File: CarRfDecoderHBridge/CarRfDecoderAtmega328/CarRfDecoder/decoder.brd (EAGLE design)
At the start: 98.7 x 80 mm, 52 parts, among them T1 BC847, T2 BC847, T3 IRLML6402, U2 RFM69CW, U3 MCP73831, U4 ATMEGA328P, U6 MIC5219 3.3V, Y1 16MHZ

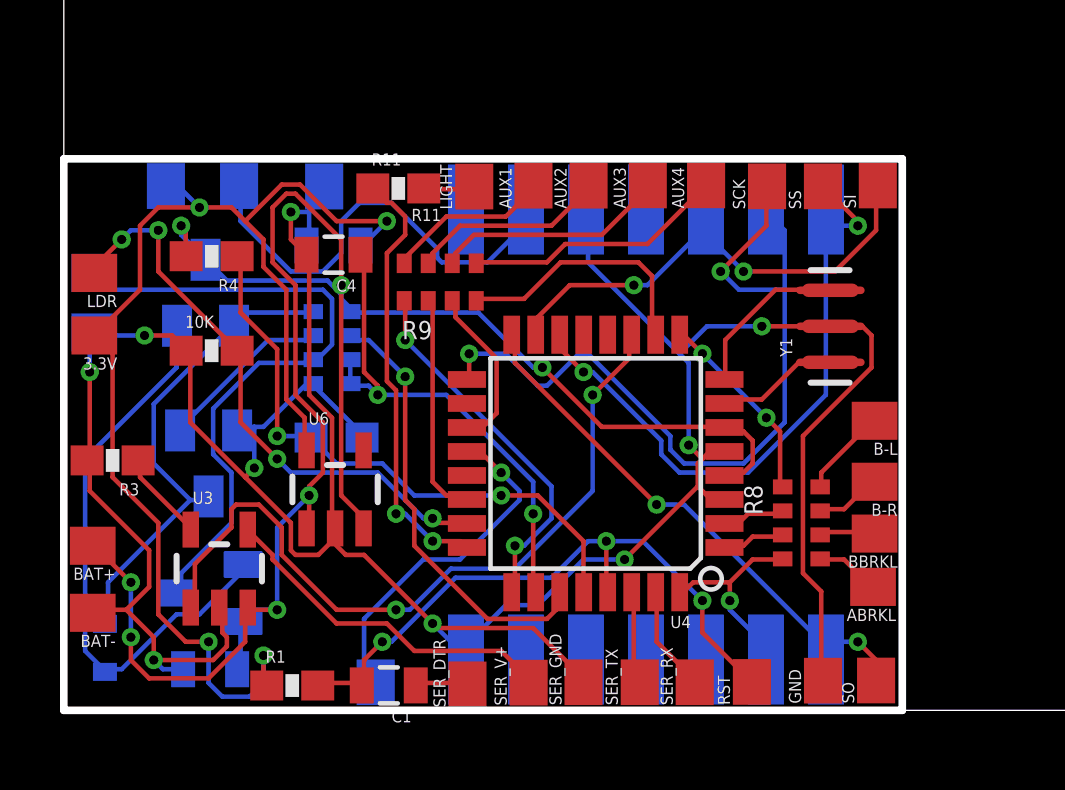
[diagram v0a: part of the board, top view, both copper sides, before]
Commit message: Add Board with hbridge
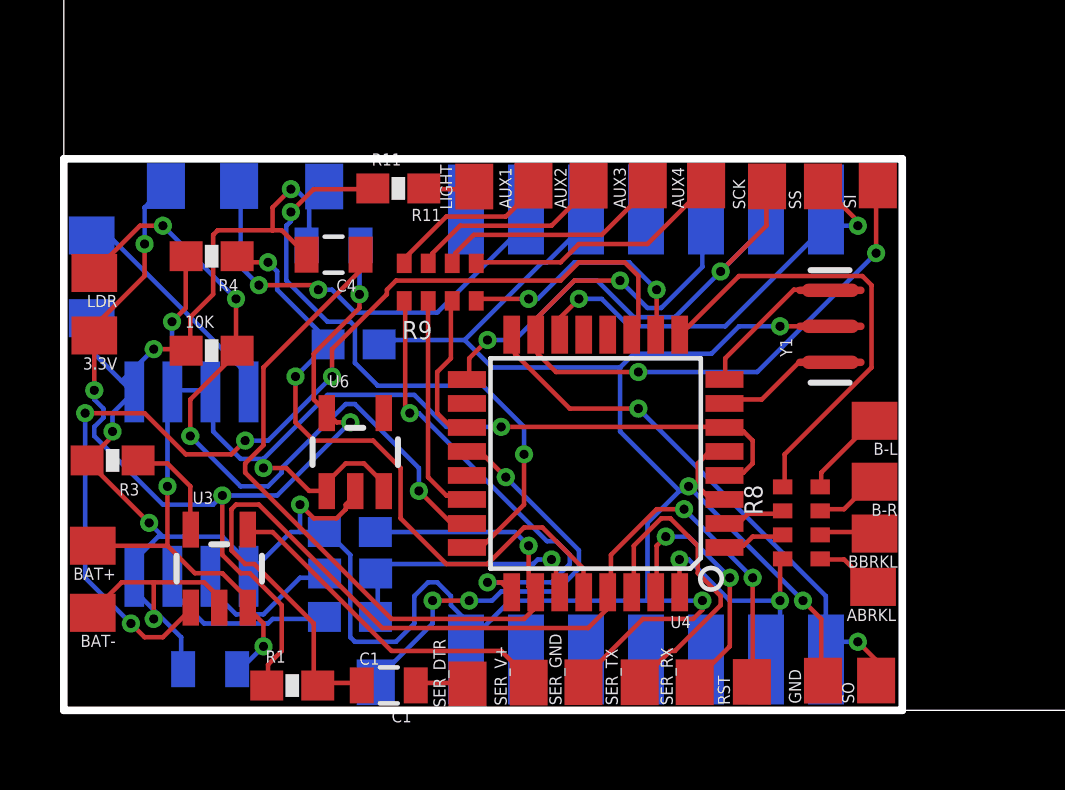
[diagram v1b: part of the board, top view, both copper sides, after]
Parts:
- removed D1: (no value), adafruit:SOD-523
- removed T1, T2: BC847, transistor:SOT23
- removed T3: IRLML6402, we-transistor:SOT23
- added MDRIVER: L9110S, h-bridge-l9119s:SO08
- added R2: 2k2, SparkFun-Resistors:0603-RES
- added R7: 0, SparkFun-Resistors:0603-RES
- R6: value 2k2 -> 0; device SparkFun-Resistors:0603-ARV -> SparkFun-Resistors:0603-RES
- moved R6 7.55 mm to (10.8, 4.56), turned to 0 degrees
- moved R5 3.16 mm to (10.9, 12.2)
- moved U6 1.41 mm to (11.0, 8.61)
- moved MOTOR 1.25 mm to (2.20, 15.8)
- moved MOTORGND 0.48 mm to (2.20, 13.1)
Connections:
- removed net N$14: D1.A, T1.2, T3.1
- removed net N$15: MOTOR.1, R6.6, T3.3
- removed net N$17: R6.7, T2.1
- removed net N$19: D1.K, R6.8, T1.1, T2.3
- new net N$6: MDRIVER.6, R6.2
- new net N$7: MDRIVER.7, R7.2
- new net OB: MDRIVER.4, MOTOR.1
- net A3: now also R2.1; no longer R6.3, R6.4
- net A4: now also R6.1, R7.1; no longer R6.2
- net BAT+: now also MDRIVER.2, MDRIVER.3; no longer R6.1, T1.3, T3.2
- net GND: now also MDRIVER.1, MDRIVER.5, MDRIVER.8, R2.2; no longer R6.5, T2.2
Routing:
- net N$15: track 21.9 -> 0.00 mm
- net BAT+: track 68.7 -> 49.0 mm, vias 7 -> 5
- net N$14: track 19.3 -> 0.00 mm
- net N$19: track 16.4 -> 0.00 mm
- net N$5: track 21.3 -> 35.1 mm, vias 3 -> 2
- net A3: track 16.9 -> 28.2 mm, vias 2 -> 1
- net SCK: track 27.8 -> 17.5 mm
- net D7: track 25.4 -> 34.8 mm, vias 2 -> 4
- net BL: track 6.59 -> 15.3 mm, vias 2 -> 0
- net MOSI: track 17.2 -> 25.6 mm, vias 2 -> 3
- net VCC: track 42.9 -> 35.0 mm, vias 4 -> 5
- net OB: track 0.00 -> 7.75 mm
- net GND: track 108.4 -> 116.0 mm, vias 9 -> 10
- net RX: track 3.09 -> 10.6 mm
- net SS: track 22.0 -> 15.4 mm
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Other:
- board text added: "C1"
- board text added: "R6"
- board text added: "R7"

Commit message: bug fixes and better board routing
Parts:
- removed SS: (no value), wirepad:SMD1,27-2,54
- moved AUX4 18.3 mm to (14.7, 0.96)
- moved AUX3 17.0 mm to (16.8, 0.96)
- moved AUX1 17.0 mm to (20.7, 0.96)
- moved AUX2 16.6 mm to (18.7, 0.92)
- moved SO 14.6 mm to (28.3, 15.6), turned to 90 degrees
- moved R9 10.0 mm to (13.1, 4.28), turned to 180 degrees
- moved SER_V+ 6.04 mm to (10.7, 0.89)
- moved SER_GND 5.98 mm to (12.6, 0.94)
- moved R7 5.97 mm to (4.85, 3.61), turned to 90 degrees
- moved C1 5.95 mm to (6.15, 0.80)
- moved SER_DTR 5.87 mm to (8.86, 0.92)
- moved R1 5.72 mm to (3.16, 0.81)
- moved R6 4.39 mm to (6.53, 3.60), turned to 90 degrees
- moved SER_RX 4.16 mm to (26.5, 0.94)
- moved SER_TX 4.16 mm to (24.6, 0.94)
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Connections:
- removed net AX1: R9.1, U4.25
- removed net AX2: R9.2, U4.22
- removed net AX3: R9.3, U4.19
- removed net AX4: R9.4, U4.10
- new net A2: R9.4, U4.25
- new net A6: C4.1, R2.1, U4.19
- new net A7: R4.1, R5.2, U4.22
- new net D6: R9.1, U4.10
- net A1: now also U3.1; no longer R11.1
- net A3: now also R9.3; no longer C4.1, R2.1
- net A5: now also R9.2; no longer R4.1, R5.2
- net D7: now also R11.1; no longer U3.1
- net SS: no longer SS.1
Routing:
- net D7: track 34.8 -> 10.3 mm, vias 4 -> 0
- net A5: track 22.1 -> 6.46 mm, vias 2 -> 0
- net AX1: track 15.3 -> 0.00 mm, vias 2 -> 0
- net A3: track 28.2 -> 13.4 mm, vias 1 -> 2
- net A6: track 0.00 -> 14.4 mm, vias 0 -> 1
- net A4: track 8.80 -> 21.9 mm
- net D6: track 0.00 -> 12.7 mm, vias 0 -> 2
- net SCK: track 17.5 -> 29.3 mm
- net A7: track 0.00 -> 11.6 mm, vias 0 -> 1
- net BAT+: track 49.0 -> 60.4 mm, vias 5 -> 9
- net A0: track 24.9 -> 15.5 mm, vias 4 -> 0
- net MISO: track 19.7 -> 28.9 mm
- net AX4: track 8.43 -> 0.00 mm, vias 2 -> 0
- net BL: track 15.3 -> 7.24 mm, vias 0 -> 2
- net A1: track 21.1 -> 13.1 mm, vias 2 -> 0
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
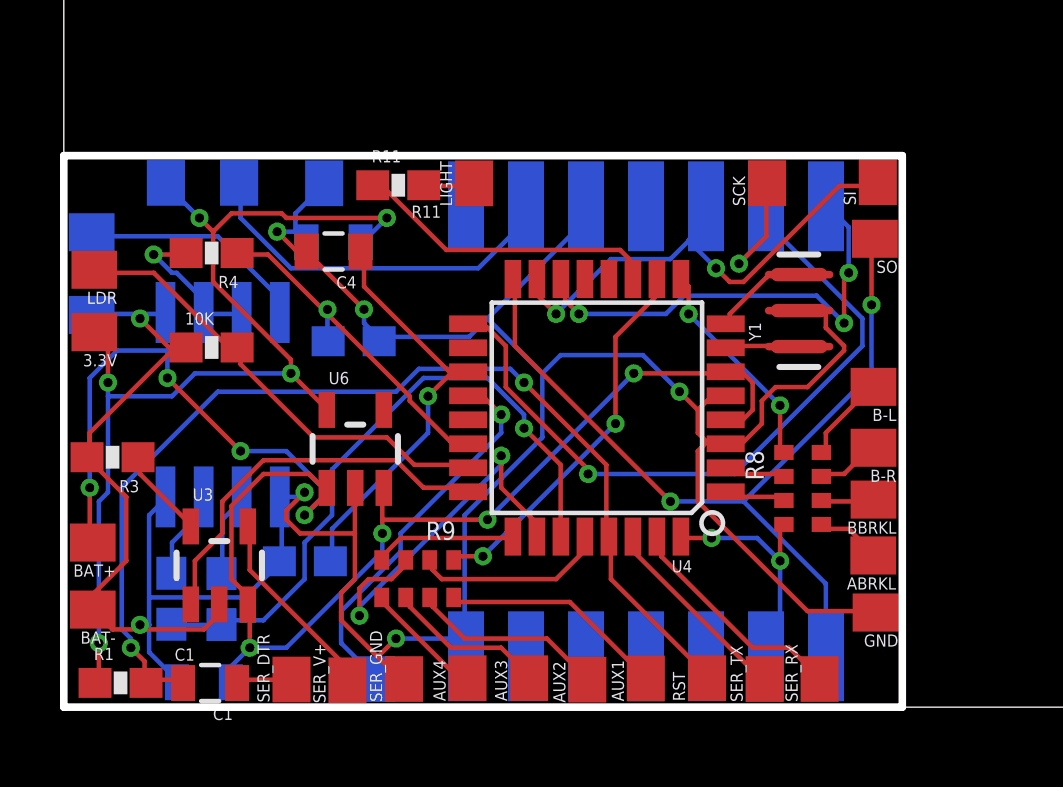
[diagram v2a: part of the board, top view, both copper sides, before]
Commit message: Add possibility to power the board from 3.3v or direct from battery.
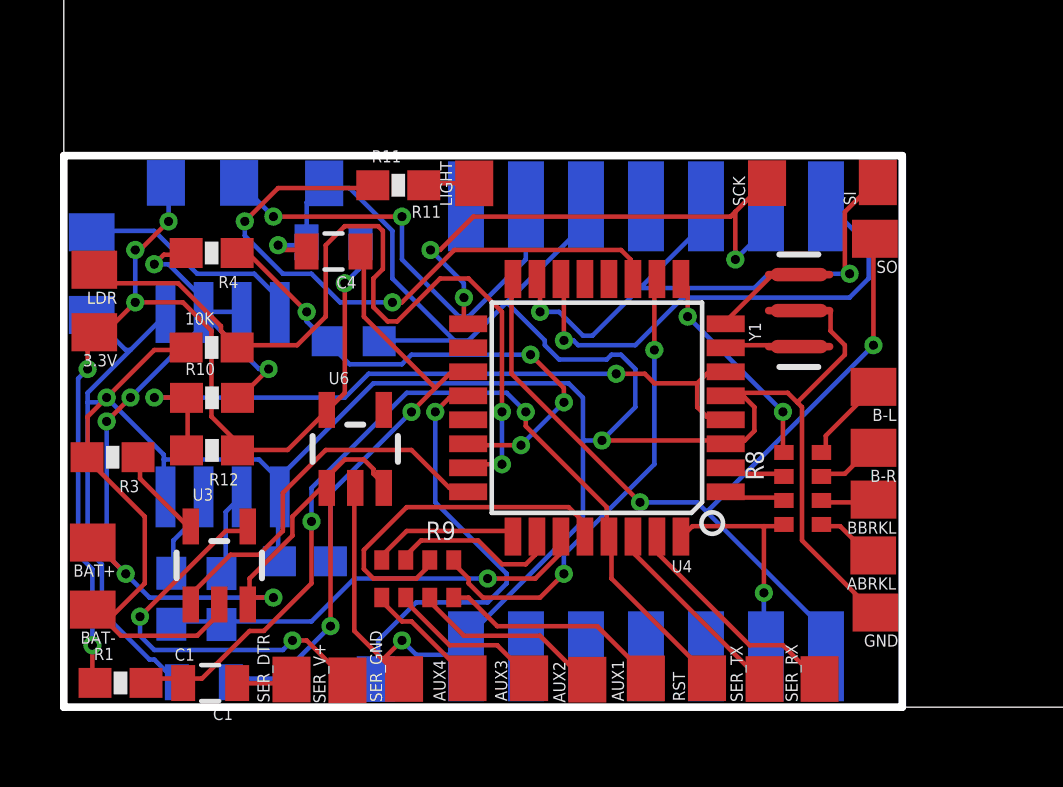
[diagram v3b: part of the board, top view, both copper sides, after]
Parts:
- added R10, R12: 0, SparkFun-Resistors:0603-RES
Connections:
- new net N$8: R10.1, R12.2, U4.4, U4.6
- net BAT+: now also R10.2; no longer U4.4, U4.6
- net VCC: now also R12.1
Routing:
- net N$8: track 0.00 -> 24.4 mm, vias 0 -> 2
- net GND: track 109.5 -> 131.9 mm, vias 7 -> 4
- net BAT+: track 60.4 -> 44.7 mm, vias 9 -> 7
- net A0: track 15.5 -> 28.5 mm, vias 0 -> 2
- net SCK: track 29.3 -> 18.9 mm, vias 2 -> 3
- net D7: track 10.3 -> 20.6 mm, vias 0 -> 2
- net A3: track 13.4 -> 5.75 mm, vias 2 -> 0
- net A4: track 21.9 -> 14.6 mm
- net N$9: track 6.52 -> 13.3 mm, vias 0 -> 2
- net A7: track 11.6 -> 17.5 mm, vias 1 -> 4
- net A5: track 6.46 -> 12.0 mm
- net N$5: track 35.8 -> 30.4 mm
- net D6: track 12.7 -> 15.8 mm
- net N$1: track 12.5 -> 14.8 mm, vias 0 -> 2
- net MOSI: track 17.8 -> 19.9 mm
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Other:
- board text removed: "R6"
- board text removed: "R7"

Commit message: Better design of board
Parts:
- added BAT+1: (no value), wirepad:SMD1,27-2,54
- added R13: 10k, SparkFun-Resistors:0603-RES
- C1: value 1uF -> 0.1uF
- moved BAT+ 1.39 mm to (2.24, 6.88)
- moved R5 1.36 mm to (11.0, 10.8)
- moved U4 0.71 mm to (19.1, 9.28)
- moved U6 0.70 mm to (11.0, 7.91)
- moved R3 0.28 mm to (2.86, 8.61)
- moved 10K 0.26 mm to (6.15, 12.2)
- moved R10 0.20 mm to (6.21, 10.5)
- moved BAT- 0.14 mm to (2.24, 3.11)
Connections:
- net BAT+: now also BAT+1.1
- net MISO: now also R13.2
- net N$1: now also R13.1
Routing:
- net GND: track 131.9 -> 121.2 mm, vias 4 -> 10
- net A1: track 12.9 -> 22.8 mm, vias 0 -> 2
- net D7: track 20.6 -> 11.4 mm
- net MISO: track 29.5 -> 37.0 mm
- net N$9: track 13.3 -> 6.50 mm, vias 2 -> 0
- net A5: track 12.0 -> 7.00 mm, vias 0 -> 2
- net A7: track 17.5 -> 12.6 mm, vias 4 -> 1
- net BAT+: track 44.7 -> 49.5 mm, vias 7 -> 2
- net A4: track 14.6 -> 19.3 mm
- net A6: track 14.1 -> 18.8 mm
- net A0: track 28.5 -> 24.2 mm, vias 2 -> 0
- net MOSI: track 19.9 -> 16.6 mm
- net D6: track 15.8 -> 12.7 mm
- net AREF: track 14.4 -> 17.4 mm
- net SS: track 16.3 -> 19.2 mm
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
